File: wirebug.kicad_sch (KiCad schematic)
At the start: 1 part

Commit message: First draft
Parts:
- added J1, J2, J3: Screw_Terminal_01x02, TerminalBlock:TerminalBlock_Altech_AK300-2_P5.00mm, symbol Connector:Screw_Terminal_01x02
- added K1: AW3211F, twyleg-misc:Relay_Panasonic_AW3211F_THT, symbol twyleg-misc:AW3211F
- added PS1: Pololu-D24V5F3, twyleg-voltage-regulators:Pololu-D24V5F3-Dev, symbol twyleg-voltage-regulators:Pololu-D24V5F3
- added Q1, Q2: BC337, Package_TO_SOT_THT:TO-92_Inline, symbol Transistor_BJT:BC337
- added R1, R2: 1K, Resistor_THT:R_Axial_DIN0207_L6.3mm_D2.5mm_P7.62mm_Horizontal, symbol Device:R
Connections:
- net SET: now reaches A1.19 (GP14|SPI1_SCK|I2C1_SDA)
- net SET: now also R1.1
- net RESET: now reaches A1.20 (GP15|SPI1_TXD|I2C1_SCL)
- net RESET: now also R2.1
- net 3V3: now reaches A1.36 (3V3(OUT))
- net 3V3: now also PS1.4 (VOUT), Q1.1 (C), Q2.1 (C)
- net GND: now reaches A1.38 (GND)
- net GND: now also K1.1, PS1.3 (GND)
- new net: Q2.2 (B), R2.2
- new net: Q1.2 (B), R1.2
- new net RESET_RELAY: K1.5, Q2.3 (E)
- new net SET_RELAY: K1.6, Q1.3 (E)
- new net VIN: PS1.2 (VIN)

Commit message: RC1
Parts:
- J1, J2, J3: footprint TerminalBlock:TerminalBlock_Altech_AK300-2_P5.00mm -> twyleg-connectors:TerminalBlock_MetzConnect_Type101_RT01602HBWC_1x02_P5.08mm_Horizontal
- R1, R2: footprint Resistor_THT:R_Axial_DIN0207_L6.3mm_D2.5mm_P7.62mm_Horizontal -> Resistor_THT:R_Axial_DIN0207_L6.3mm_D2.5mm_P2.54mm_Vertical
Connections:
- net GND: now also A1.13 (GND), A1.18 (GND), A1.23 (GND), A1.28 (GND), A1.3 (GND), A1.33 (GND|AGND), A1.8 (GND), J3.2 (Pin_2)
- net VIN: now also J3.1 (Pin_1)
- net SIG_IN: now reaches J1.1 (Pin_1)
- net SIG_IN: now also J1.2 (Pin_2), K1.3
- net SIG_OUT: now reaches K1.4
- net SIG_OUT: now also J2.1 (Pin_1), J2.2 (Pin_2)
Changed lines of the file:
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@@
+    (stroke (width 0) (type default))
+  )
+  (wire (pts (xy 242.57 25.4) (xy 242.57 30.48))
+    (stroke (width 0) (type default))
+  )
+  (wire (pts (xy 43.18 31.75) (xy 48.26 31.75))
+    (stroke (width 0) (type default))
+  )
+  (wire (pts (xy 100.33 85.09) (xy 93.98 85.09))
     (stroke (width 0) (type default))
   )
@@
     (stroke (width 0) (type default))
   )
+  (wire (pts (xy 100.33 72.39) (xy 93.98 72.39))
+    (stroke (width 0) (type default))
+  )
   (wire (pts (xy 250.19 109.22) (xy 254 109.22))
     (stroke (width 0) (type default))
@@
     (stroke (width 0) (type default))
   )
+  (wire (pts (xy 100.33 97.79) (xy 93.98 97.79))
+    (stroke (width 0) (type default))
+  )
+  (wire (pts (xy 100.33 59.69) (xy 93.98 59.69))
+    (stroke (width 0) (type default))
+  )
   (wire (pts (xy 231.14 45.72) (xy 231.14 49.53))
     (stroke (width 0) (type default))
   )
+  (wire (pts (xy 43.18 36.83) (xy 48.26 36.83))
+    (stroke (width 0) (type default))
+  )
+  (wire (pts (xy 180.34 85.09) (xy 186.69 85.09))
+    (stroke (width 0) (type default))
+  )
+  (wire (pts (xy 43.18 29.21) (xy 48.26 29.21))
+    (stroke (width 0) (type default))
+  )
+  (wire (pts (xy 43.18 39.37) (xy 48.26 39.37))
+    (stroke (width 0) (type default))
+  )
   (wire (pts (xy 68.58 148.59) (xy 68.58 152.4))
     (stroke (width 0) (type default))
@@
     (stroke (width 0) (type default))
   )
+  (wire (pts (xy 43.18 21.59) (xy 48.26 21.59))
+    (stroke (width 0) (type default))
+  )
+  (wire (pts (xy 240.03 25.4) (xy 240.03 30.48))
+    (stroke (width 0) (type default))
+  )
+  (wire (pts (xy 43.18 24.13) (xy 48.26 24.13))
+    (stroke (width 0) (type default))
+  )
   (wire (pts (xy 44.45 143.51) (xy 53.34 143.51))
     (stroke (width 0) (type default))
   )
+  (wire (pts (xy 180.34 97.79) (xy 186.69 97.79))
+    (stroke (width 0) (type default))
+  )
+  (wire (pts (xy 180.34 72.39) (xy 186.69 72.39))
+    (stroke (width 0) (type default))
+  )
   (wire (pts (xy 228.6 45.72) (xy 228.6 49.53))
     (stroke (width 0) (type default))
@@
     (effects (font (size 1.27 1.27)) (justify right bottom))
   )
+  (label "VIN" (at 43.18 36.83 180) (fields_autoplaced)
+    (effects (font (size 1.27 1.27)) (justify right bottom))
+  )
+  (label "SIG_IN" (at 43.18 21.59 180) (fields_autoplaced)
+    (effects (font (size 1.27 1.27)) (justify right bottom))
+  )
+  (label "GND" (at 186.69 72.39 0) (fields_autoplaced)
+    (effects (font (size 1.27 1.27)) (justify left bottom))
+  )
   (label "RESET_RELAY" (at 109.22 152.4 270) (fields_autoplaced)
     (effects (font (size 1.27 1.27)) (justify right bottom))
@@
     (effects (font (size 1.27 1.27)) (justify right bottom))
   )
+  (label "SIG_IN" (at 43.18 24.13 180) (fields_autoplaced)
+    (effects (font (size 1.27 1.27)) (justify right bottom))
+  )
+  (label "SIG_OUT" (at 43.18 31.75 180) (fields_autoplaced)
+    (effects (font (size 1.27 1.27)) (justify right bottom))
+  )
   (label "SET_RELAY" (at 68.58 152.4 270) (fields_autoplaced)
     (effects (font (size 1.27 1.27)) (justify right bottom))
@@
     (effects (font (size 1.27 1.27)) (justify left bottom))
   )
+  (label "GND" (at 93.98 59.69 180) (fields_autoplaced)
+    (effects (font (size 1.27 1.27)) (justify right bottom))
+  )
+  (label "GND" (at 186.69 97.79 0) (fields_autoplaced)
+    (effects (font (size 1.27 1.27)) (justify left bottom))
+  )
   (label "RESET" (at 93.98 102.87 180) (fields_autoplaced)
     (effects (font (size 1.27 1.27)) (justify right bottom))
@@
     (effects (font (size 1.27 1.27)) (justify right bottom))
   )
+  (label "GND" (at 93.98 72.39 180) (fields_autoplaced)
+    (effects (font (size 1.27 1.27)) (justify right bottom))
+  )
+  (label "GND" (at 186.69 85.09 0) (fields_autoplaced)
+    (effects (font (size 1.27 1.27)) (justify left bottom))
+  )
+  (label "SIG_OUT" (at 43.18 29.21 180) (fields_autoplaced)
+    (effects (font (size 1.27 1.27)) (justify right bottom))
+  )
+  (label "SIG_IN" (at 240.03 25.4 90) (fields_autoplaced)
+    (effects (font (size 1.27 1.27)) (justify left bottom))
+  )
   (label "GND" (at 186.69 59.69 0) (fields_autoplaced)
     (effects (font (size 1.27 1.27)) (justify left bottom))
   )
+  (label "GND" (at 93.98 85.09 180) (fields_autoplaced)
+    (effects (font (size 1.27 1.27)) (justify right bottom))
+  )
   (label "RESET" (at 86.36 143.51 0) (fields_autoplaced)
     (effects (font (size 1.27 1.27)) (justify left bottom))
   )
+  (label "SIG_OUT" (at 242.57 25.4 90) (fields_autoplaced)
+    (effects (font (size 1.27 1.27)) (justify left bottom))
+  )
   (label "RESET_RELAY" (at 231.14 49.53 270) (fields_autoplaced)
     (effects (font (size 1.27 1.27)) (justify right bottom))
   )
+  (label "GND" (at 43.18 39.37 180) (fields_autoplaced)
+    (effects (font (size 1.27 1.27)) (justify right bottom))
+  )
   (label "3V3" (at 254 109.22 0) (fields_autoplaced)
     (effects (font (size 1.27 1.27)) (justify left bottom))
   )
+  (label "GND" (at 93.98 97.79 180) (fields_autoplaced)
+    (effects (font (size 1.27 1.27)) (justify right bottom))
+  )
   (symbol (lib_id "Connector:Screw_Terminal_01x02") (at 53.34 36.83 0) (unit 1)
     (in_bom yes) (on_board yes) (dnp no) (fields_autoplaced)
@@
       (effects (font (size 1.27 1.27)) (justify left))
     )
-    (property "Footprint" "TerminalBlock:TerminalBlock_Altech_AK300-2_P5.00mm" (at 53.34 36.83 0)
+    (property "Footprint" "twyleg-connectors:TerminalBlock_MetzConnect_Type101_RT01602HBWC_1x02_P5.08mm_Horizontal" (at 53.34 36.83 0)
       (effects (font (size 1.27 1.27)) hide)
     )
@@
       (effects (font (size 1.27 1.27)) (justify left))
     )
-    (property "Footprint" "TerminalBlock:TerminalBlock_Altech_AK300-2_P5.00mm" (at 53.34 21.59 0)
+    (property "Footprint" "twyleg-connectors:TerminalBlock_MetzConnect_Type101_RT01602HBWC_1x02_P5.08mm_Horizontal" (at 53.34 21.59 0)
       (effects (font (size 1.27 1.27)) hide)
     )
@@
       (effects (font (size 1.27 1.27)))
     )
-    (property "Footprint" "Resistor_THT:R_Axial_DIN0207_L6.3mm_D2.5mm_P7.62mm_Horizontal" (at 97.79 145.288 90)
+    (property "Footprint" "Resistor_THT:R_Axial_DIN0207_L6.3mm_D2.5mm_P2.54mm_Vertical" (at 97.79 145.288 90)
       (effects (font (size 1.27 1.27)) hide)
     )
@@
       (effects (font (size 1.27 1.27)) (justify left))
     )
-    (property "Footprint" "TerminalBlock:TerminalBlock_Altech_AK300-2_P5.00mm" (at 53.34 29.21 0)
+    (property "Footprint" "twyleg-connectors:TerminalBlock_MetzConnect_Type101_RT01602HBWC_1x02_P5.08mm_Horizontal" (at 53.34 29.21 0)
       (effects (font (size 1.27 1.27)) hide)
     )
@@
       (effects (font (size 1.27 1.27)))
     )
-    (property "Footprint" "Resistor_THT:R_Axial_DIN0207_L6.3mm_D2.5mm_P7.62mm_Horizontal" (at 57.15 145.288 90)
-      (effects (font (size 1.27 1.27)) hide)
-    )
+    (property "Footprint" "Resistor_THT:R_Axial_DIN0207_L6.3mm_D2.5mm_P2.54mm_Vertical" (at 57.15 145.288 90)
+      (effects (font (size 1.27 1.27)) hide)
+    )

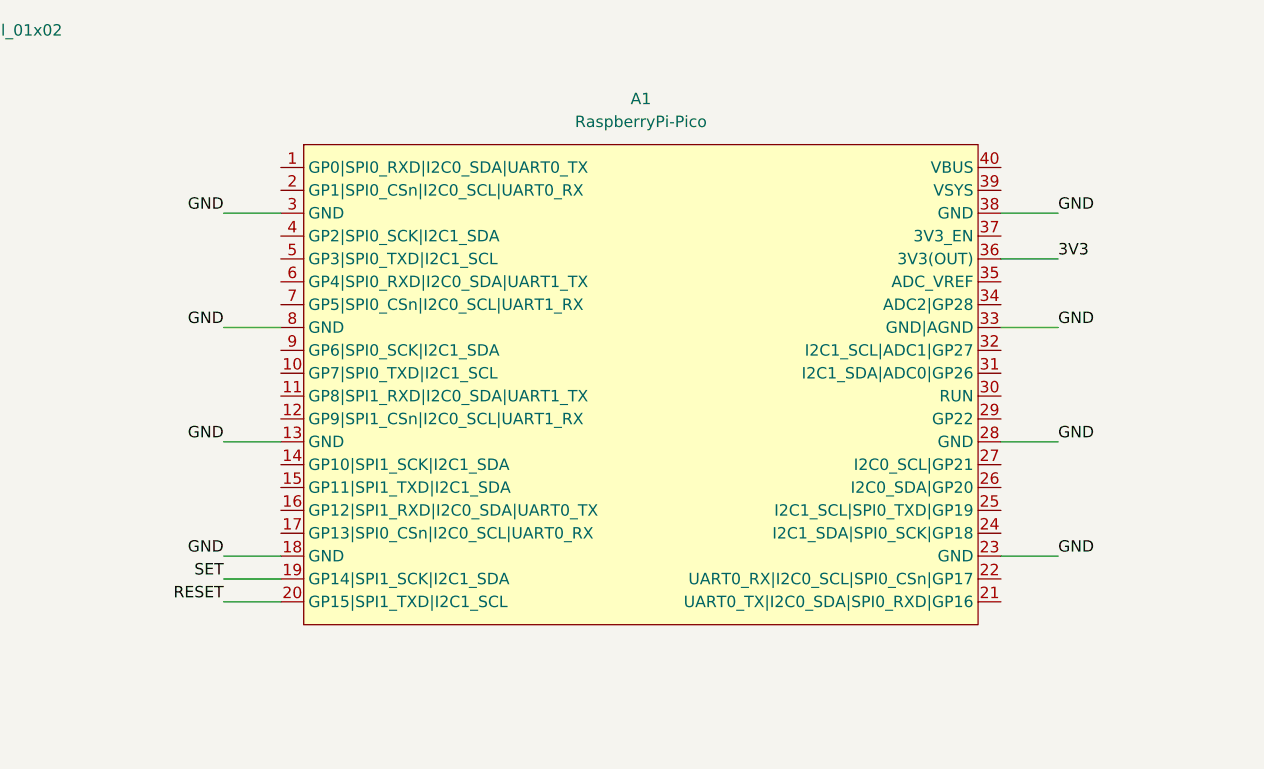
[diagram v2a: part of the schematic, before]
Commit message: Updated PicoW and voltage regultator
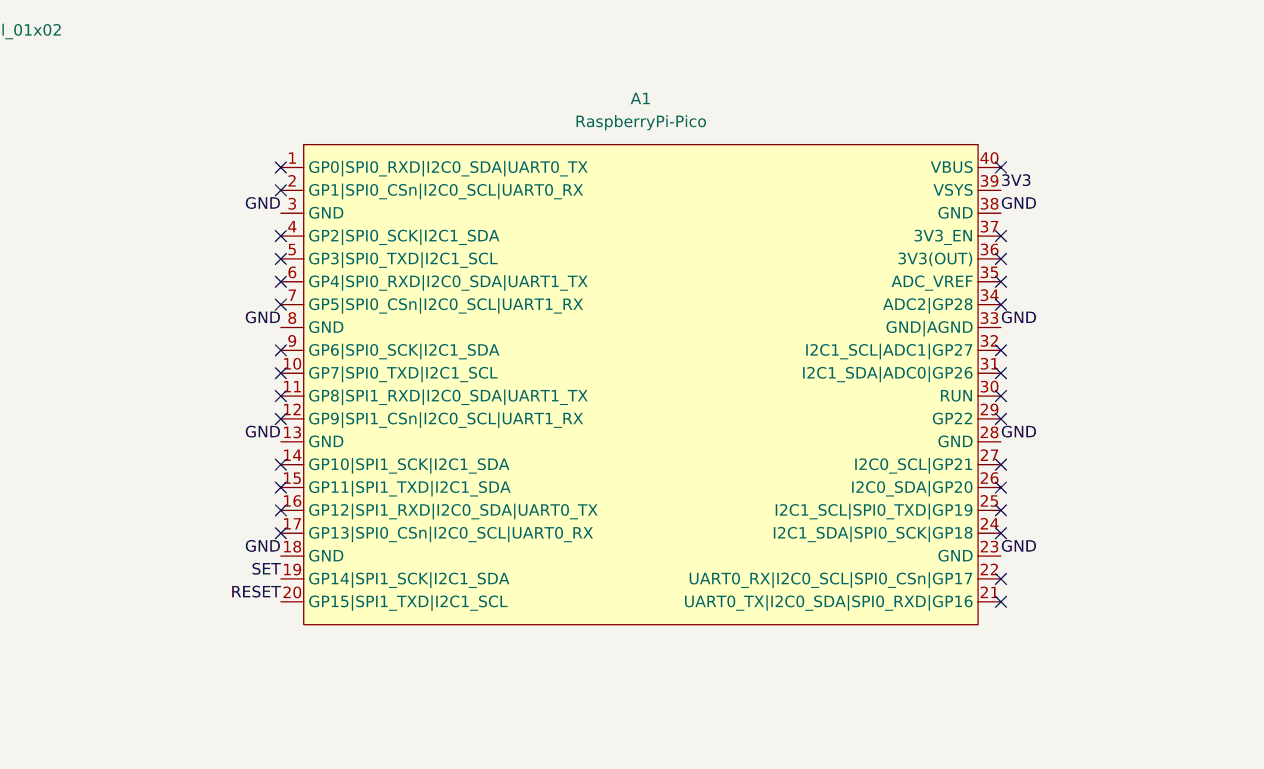
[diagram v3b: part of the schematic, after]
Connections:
- net 3V3: now also A1.39 (VSYS); no longer A1.36 (3V3(OUT))
- no-connect marks 0 -> 29
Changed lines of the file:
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@@
 (kicad_sch (version 20230121) (generator eeschema)
   (paper "A4")
-  (wire (pts (xy 180.34 59.69) (xy 186.69 59.69))
-    (stroke (width 0) (type default))
-  )
+  (no_connect (at 180.34 62.23))
+  (no_connect (at 180.34 69.85))
+  (no_connect (at 180.34 64.77))
+  (no_connect (at 180.34 54.61))
+  (no_connect (at 180.34 74.93))
+  (no_connect (at 100.33 62.23))
+  (no_connect (at 180.34 100.33))
+  (no_connect (at 180.34 95.25))
+  (no_connect (at 100.33 54.61))
+  (no_connect (at 100.33 67.31))
+  (no_connect (at 100.33 82.55))
+  (no_connect (at 100.33 57.15))
+  (no_connect (at 180.34 67.31))
+  (no_connect (at 100.33 87.63))
+  (no_connect (at 100.33 77.47))
+  (no_connect (at 180.34 77.47))
+  (no_connect (at 100.33 95.25))
+  (no_connect (at 180.34 80.01))
+  (no_connect (at 100.33 80.01))
+  (no_connect (at 180.34 90.17))
+  (no_connect (at 180.34 82.55))
+  (no_connect (at 100.33 92.71))
+  (no_connect (at 180.34 102.87))
+  (no_connect (at 100.33 64.77))
+  (no_connect (at 100.33 69.85))
+  (no_connect (at 100.33 74.93))
+  (no_connect (at 180.34 92.71))
+  (no_connect (at 100.33 90.17))
+  (no_connect (at 180.34 87.63))
   (wire (pts (xy 242.57 25.4) (xy 242.57 30.48))
     (stroke (width 0) (type default))
@@
     (stroke (width 0) (type default))
   )
-  (wire (pts (xy 100.33 85.09) (xy 93.98 85.09))
-    (stroke (width 0) (type default))
-  )
   (wire (pts (xy 109.22 148.59) (xy 109.22 152.4))
-    (stroke (width 0) (type default))
-  )
-  (wire (pts (xy 93.98 100.33) (xy 100.33 100.33))
-    (stroke (width 0) (type default))
-  )
-  (wire (pts (xy 100.33 72.39) (xy 93.98 72.39))
     (stroke (width 0) (type default))
   )
@@
     (stroke (width 0) (type default))
   )
-  (wire (pts (xy 100.33 97.79) (xy 93.98 97.79))
-    (stroke (width 0) (type default))
-  )
-  (wire (pts (xy 100.33 59.69) (xy 93.98 59.69))
-    (stroke (width 0) (type default))
-  )
   (wire (pts (xy 231.14 45.72) (xy 231.14 49.53))
     (stroke (width 0) (type default))
   )
   (wire (pts (xy 43.18 36.83) (xy 48.26 36.83))
-    (stroke (width 0) (type default))
-  )
-  (wire (pts (xy 180.34 85.09) (xy 186.69 85.09))
     (stroke (width 0) (type default))
   )
@@
     (stroke (width 0) (type default))
   )
-  (wire (pts (xy 180.34 64.77) (xy 186.69 64.77))
-    (stroke (width 0) (type default))
-  )
   (wire (pts (xy 222.25 109.22) (xy 226.06 109.22))
-    (stroke (width 0) (type default))
-  )
-  (wire (pts (xy 93.98 102.87) (xy 100.33 102.87))
     (stroke (width 0) (type default))
   )
@@
   )
   (wire (pts (xy 44.45 143.51) (xy 53.34 143.51))
-    (stroke (width 0) (type default))
-  )
-  (wire (pts (xy 180.34 97.79) (xy 186.69 97.79))
-    (stroke (width 0) (type default))
-  )
-  (wire (pts (xy 180.34 72.39) (xy 186.69 72.39))
     (stroke (width 0) (type default))
   )
@@
     (effects (font (size 1.27 1.27)) (justify right bottom))
   )
-  (label "GND" (at 186.69 72.39 0) (fields_autoplaced)
+  (label "GND" (at 180.34 72.39 0) (fields_autoplaced)
     (effects (font (size 1.27 1.27)) (justify left bottom))
   )
@@
     (effects (font (size 1.27 1.27)) (justify right bottom))
   )
-  (label "SET" (at 93.98 100.33 180) (fields_autoplaced)
+  (label "SET" (at 100.33 100.33 180) (fields_autoplaced)
     (effects (font (size 1.27 1.27)) (justify right bottom))
   )
@@
     (effects (font (size 1.27 1.27)) (justify right bottom))
   )
-  (label "3V3" (at 186.69 64.77 0) (fields_autoplaced)
+  (label "3V3" (at 180.34 57.15 0) (fields_autoplaced)
     (effects (font (size 1.27 1.27)) (justify left bottom))
   )
-  (label "GND" (at 93.98 59.69 180) (fields_autoplaced)
+  (label "GND" (at 100.33 59.69 180) (fields_autoplaced)
     (effects (font (size 1.27 1.27)) (justify right bottom))
   )
-  (label "GND" (at 186.69 97.79 0) (fields_autoplaced)
+  (label "GND" (at 180.34 97.79 0) (fields_autoplaced)
     (effects (font (size 1.27 1.27)) (justify left bottom))
   )
-  (label "RESET" (at 93.98 102.87 180) (fields_autoplaced)
+  (label "RESET" (at 100.33 102.87 180) (fields_autoplaced)
     (effects (font (size 1.27 1.27)) (justify right bottom))
   )
@@
     (effects (font (size 1.27 1.27)) (justify right bottom))
   )
-  (label "GND" (at 93.98 72.39 180) (fields_autoplaced)
+  (label "GND" (at 100.33 72.39 180) (fields_autoplaced)
     (effects (font (size 1.27 1.27)) (justify right bottom))
   )
-  (label "GND" (at 186.69 85.09 0) (fields_autoplaced)
+  (label "GND" (at 180.34 85.09 0) (fields_autoplaced)
     (effects (font (size 1.27 1.27)) (justify left bottom))
   )
@@
     (effects (font (size 1.27 1.27)) (justify left bottom))
   )
-  (label "GND" (at 186.69 59.69 0) (fields_autoplaced)
+  (label "GND" (at 180.34 59.69 0) (fields_autoplaced)
     (effects (font (size 1.27 1.27)) (justify left bottom))
   )
-  (label "GND" (at 93.98 85.09 180) (fields_autoplaced)
+  (label "GND" (at 100.33 85.09 180) (fields_autoplaced)
     (effects (font (size 1.27 1.27)) (justify right bottom))
   )
@@
     (effects (font (size 1.27 1.27)) (justify left bottom))
   )
-  (label "GND" (at 93.98 97.79 180) (fields_autoplaced)
+  (label "GND" (at 100.33 97.79 180) (fields_autoplaced)
     (effects (font (size 1.27 1.27)) (justify right bottom))
   )
